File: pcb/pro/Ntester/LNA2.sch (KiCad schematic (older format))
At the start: 21 parts, among them Q3 BC847BDW1T1G, U6 LT1818

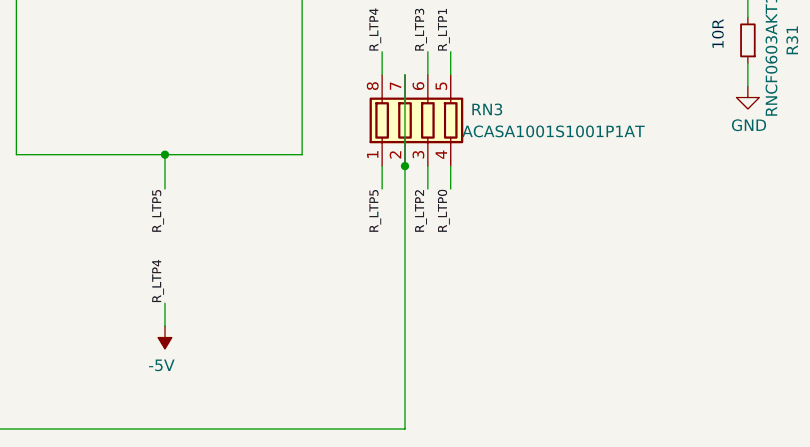
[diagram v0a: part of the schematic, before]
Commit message: BOM was updated
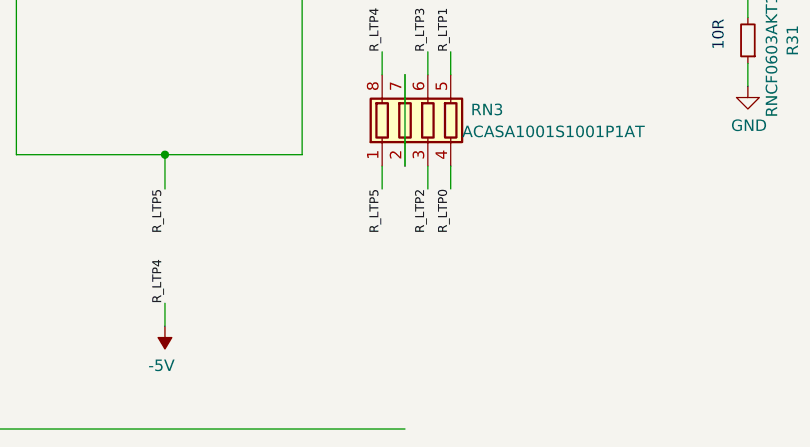
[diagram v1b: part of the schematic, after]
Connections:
- net IN_AMP: no longer RN3.2 (R2.1), RN3.7 (R2.2)
- new net: RN3.2 (R2.1), RN3.7 (R2.2)
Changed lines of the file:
@@
 	4699 4222 4699 4622
-Wire Wire Line
-	4699 4622 4699 5772
 Wire Wire Line
 	4699 5772 2599 5772
 Wire Wire Line
 	2599 5772 2599 3672
-Connection ~ 4699 4622
 Connection ~ 2599 3672
 Wire Wire Line
